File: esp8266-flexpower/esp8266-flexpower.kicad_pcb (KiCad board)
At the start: 4 copper layers, 70 x 62 mm, 101 parts, among them Q1 2N7002, Q2 MMBT3904, Q3 MMBT3904, Q4 2N7002, SW1 B3U-1000P, SW2 B3U-1000P, U1 TPS63070RNMR, U2 USBLC6-2SC6, U3 CH340C, U4 ESP-12F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

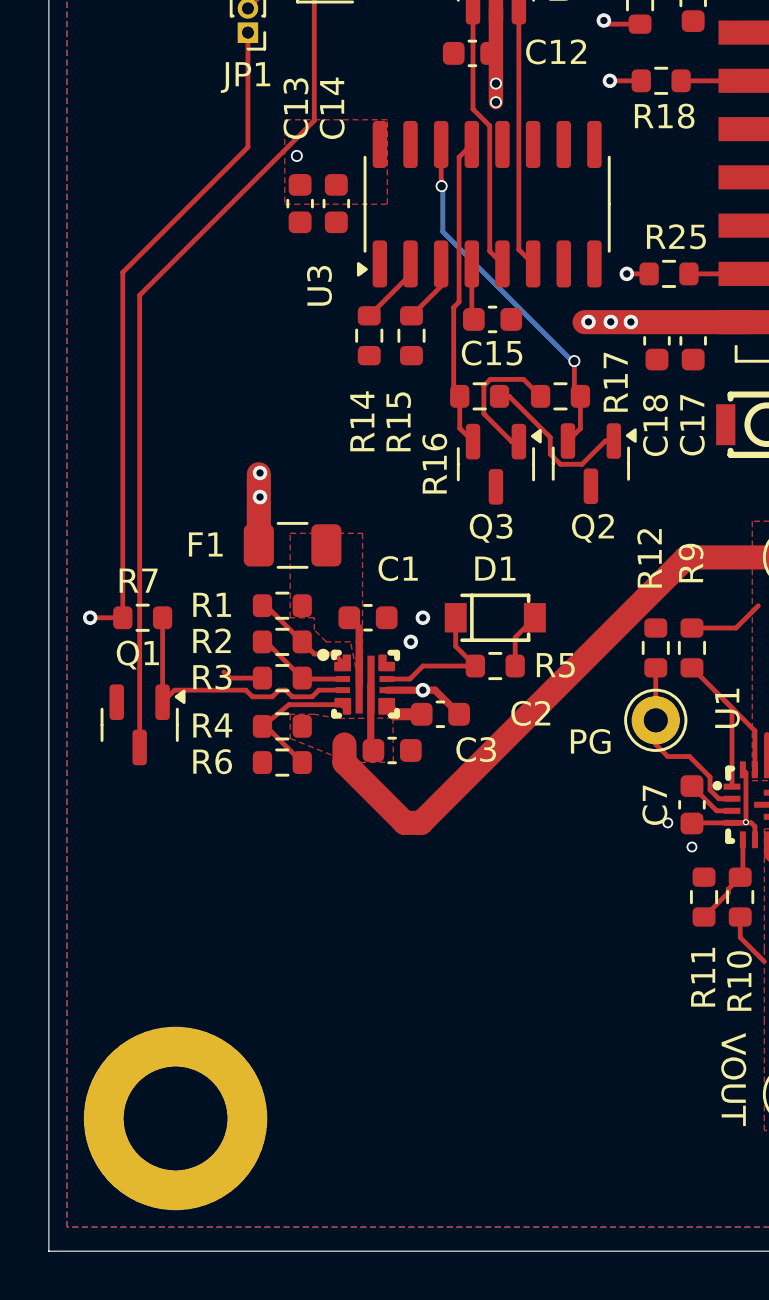
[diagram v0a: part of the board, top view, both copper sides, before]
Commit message: add qwiic connector
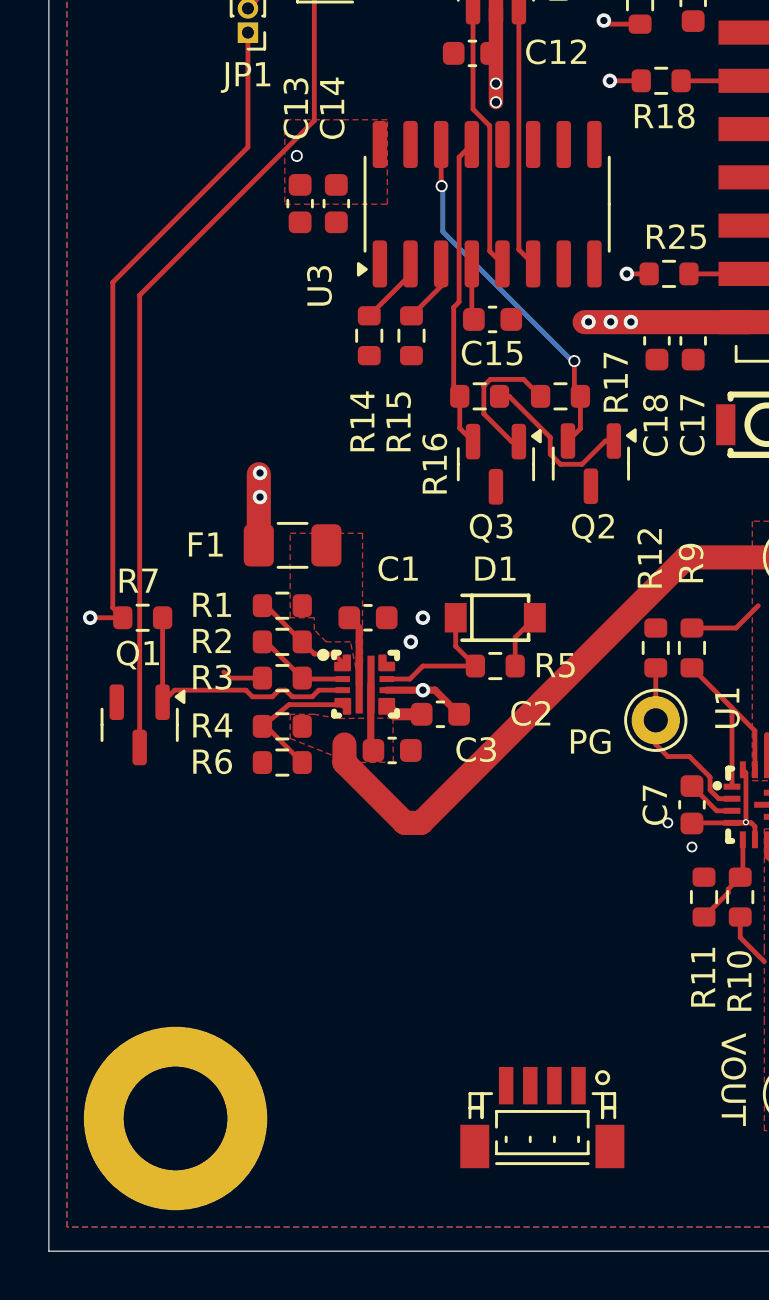
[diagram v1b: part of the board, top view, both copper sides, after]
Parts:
- added CN1: BM04B-SRSS-TB(LF)(SN), easyeda2kicad:CONN-SMD_BM04B-SRSS-TB, F.Cu at (34.2, 69.4)

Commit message: ready to fab
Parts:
- added C22: 6.8uf, Capacitor_SMD:C_0603_1608Metric, F.Cu at (62.7, 45.9)
- added C23: 10uf, Capacitor_SMD:C_0603_1608Metric, F.Cu at (60.7, 42.7)
- added C24: 0.1uf, Capacitor_SMD:C_0603_1608Metric, F.Cu at (60.7, 45.9)
- added C25: 10uf, Capacitor_SMD:C_0603_1608Metric, F.Cu at (27.9, 59.9)
- added C26: 10uf, Capacitor_SMD:C_0603_1608Metric, F.Cu at (23.7, 59.9)
- added C27: 47uf, Capacitor_SMD:C_0603_1608Metric, F.Cu at (64.8, 42.2)
- added CN2: BM04B-SRSS-TB(LF)(SN), easyeda2kicad:CONN-SMD_BM04B-SRSS-TB, F.Cu at (61.8, 71.0)
- added CN3: BM04B-SRSS-TB(LF)(SN), easyeda2kicad:CONN-SMD_BM04B-SRSS-TB, F.Cu at (54.6, 71.0)
- added U7: SPX3940AM3-L-3-3/TR, easyeda2kicad:SOT-223-3_L6.5-W3.4-P2.30-LS7.0-BR, F.Cu at (55.4, 44.2)
- added U8: AMS1117-5.0_C347223, easyeda2kicad:SOT-223_L6.7-W3.5-P2.30-BR, F.Cu at (26.8, 65.0)
- added U9: B3B-XH-A(LF)(SN), easyeda2kicad:CONN-TH_3P-P2.50_A2501WV2-3P, F.Cu at (36.3, 69.6)
- JP1, JP2: footprint Connector_PinHeader_1.00mm:PinHeader_1x02_P1.00mm_Vertical -> Jumper:SolderJumper-2_P1.3mm_Bridged_Pad1.0x1.5mm
- R14, R15: value 480 -> 470
- moved CN1 35.0 mm to (69.2, 71.0)
- moved SW2 7.10 mm to (49.4, 40.8)
- moved C17 1.50 mm to (39.0, 37.3)
- moved C18 1.50 mm to (40.5, 37.3)
- moved JP2 1.05 mm to (70.6, 40.0), turned to 90 degrees
- moved JP1 1.00 mm to (21.0, 24.5)
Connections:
- net /ESP12F/3V3 renamed /33Reg/VOUT
- C10 pad 1: /BB6V/VOUT -> /33Reg/VIN
- C11 pad 1: /BB6V/VOUT -> /33Reg/VIN
- C8 pad 1: /BB6V/VOUT -> /33Reg/VIN
- C9 pad 1: /BB6V/VOUT -> /33Reg/VIN
- CN1 pad 1: unconnected-(CN1-Pad1) -> GND
- CN1 pad 2: unconnected-(CN1-Pad2) -> /33Reg/VIN
- CN1 pad 3: unconnected-(CN1-Pad3) -> /ESP12F/SDA
- CN1 pad 4: unconnected-(CN1-Pad4) -> /ESP12F/SCL
- D7 pad 1: /PP3V16V1/IMON -> /LEDComparator/Input
- Protect2 pad 9: /PP3V16V1/IMON -> /LEDComparator/Input
- Q2 pad 3: /usb_serial/RST -> /ESP12F/RST
- Q3 pad 3: /usb_serial/BOOT -> /ESP12F/BOOT
- R10 pad 1: /BB6V/VOUT -> /33Reg/VIN
- R12 pad 1: /BB6V/VLogic -> +5V
- R14 pad 2: /usb_serial/TXD -> /ESP12F/RXD
- R15 pad 1: /usb_serial/RXD -> /ESP12F/TXD
- R42 pad 2: /PP3V16V1/IMON -> /LEDComparator/Input
- TP3 pad 1: /BB6V/VOUT -> /33Reg/VIN
- U1 pad 7: /BB6V/VOUT -> /33Reg/VIN
- U1 pad 8: /BB6V/VOUT -> /33Reg/VIN
- U5 pad 10: Net-(U5A--) -> /LEDComparator/Input
- U5 pad 4: Net-(U5A--) -> /LEDComparator/Input
- U5 pad 6: Net-(U5A--) -> /LEDComparator/Input
- U5 pad 8: Net-(U5A--) -> /LEDComparator/Input
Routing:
- net /33Reg/VOUT: track 16.3 -> 89.7 mm, vias 10 -> 12
- net /ESP12F/SCL: track 8.92 -> 70.6 mm, vias 0 -> 2
- net /ESP12F/SDA: track 8.92 -> 68.0 mm, vias 0 -> 2
- net /33Reg/VIN: track 0.00 -> 50.7 mm, vias 0 -> 3
- net /ESP12F/TXD: track 0.00 -> 47.5 mm, vias 0 -> 2
- net /ESP12F/RXD: track 0.00 -> 45.7 mm, vias 0 -> 2
- net /ESP12F/ONEW: track 2.48 -> 42.3 mm, vias 0 -> 1
- net /LEDComparator/Input: track 0.00 -> 39.2 mm, vias 0 -> 2
- net /ESP12F/BOOT: track 21.1 -> 47.4 mm
- net +5V: track 41.8 -> 54.2 mm, vias 11 -> 14
- net Net-(U5A--): track 12.3 -> 0.00 mm
- net /ESP12F/RST: track 24.6 -> 33.9 mm
- net /PP3V16V1/IMON: track 6.24 -> 0.00 mm
- net /BB6V/VOUT: track 3.48 -> 0.00 mm
- net Net-(JP1-B): track 3.71 -> 6.33 mm
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- added copper zone on F.Cu, net /33Reg/VIN
- added copper zone on In2.Cu, net /33Reg/VIN
- removed copper zone on F.Cu, net /BB6V/VOUT
- removed copper zone on In2.Cu, net /BB6V/VOUT
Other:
- board text added: "3V I2C"
- board text added: "5V I2C"
- board text added: "6V I2C"
- board text added: "TEMP"
